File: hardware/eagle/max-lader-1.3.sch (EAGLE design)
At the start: 69 parts, among them IC1 OPA343, IC2 LM385-2.5, IC3 ICL 7667, IC4 7805, IC5 MEGA168-P, Q1 IRF4905, Q2 16MHz, Q3 IRFZ 48N, Q4 IRFZ 48N

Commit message: eagle files
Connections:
- net N$1 renamed INPUT_GATE
- net N$10 renamed BOOST_GATE
- net N$15 renamed BOOST_CTRL
- net N$3 renamed BUCK_CTRL
- net N$4 renamed BUCK_GATE
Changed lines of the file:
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@@
 <?xml version="1.0" encoding="utf-8"?>
 <!DOCTYPE eagle SYSTEM "eagle.dtd">
-<eagle version="6.5.0">
+<eagle version="7.7.0">
 <drawing>
 <settings>
@@
 </segment>
 </net>
-<net name="N$15" class="0">
+<net name="BOOST_CTRL" class="0">
 <segment>
 <wire x1="93.98" y1="17.78" x2="93.98" y2="40.64" width="0.1524" layer="91"/>
@@
 </segment>
 </net>
-<net name="N$1" class="0">
+<net name="INPUT_GATE" class="0">
 <segment>
 <wire x1="-17.78" y1="48.26" x2="-12.7" y2="48.26" width="0.1524" layer="91"/>
@@
 </segment>
 </net>
-<net name="N$10" class="0">
+<net name="BOOST_GATE" class="0">
 <segment>
 <wire x1="93.98" y1="53.34" x2="101.6" y2="53.34" width="0.1524" layer="91"/>
@@
 </segment>
 </net>
-<net name="N$4" class="0">
+<net name="BUCK_GATE" class="0">
 <segment>
 <wire x1="73.66" y1="78.74" x2="66.04" y2="78.74" width="0.1524" layer="91"/>
@@
 </segment>
 </net>
-<net name="N$3" class="0">
+<net name="BUCK_CTRL" class="0">
 <segment>
 <wire x1="66.04" y1="38.1" x2="66.04" y2="22.86" width="0.1524" layer="91"/>

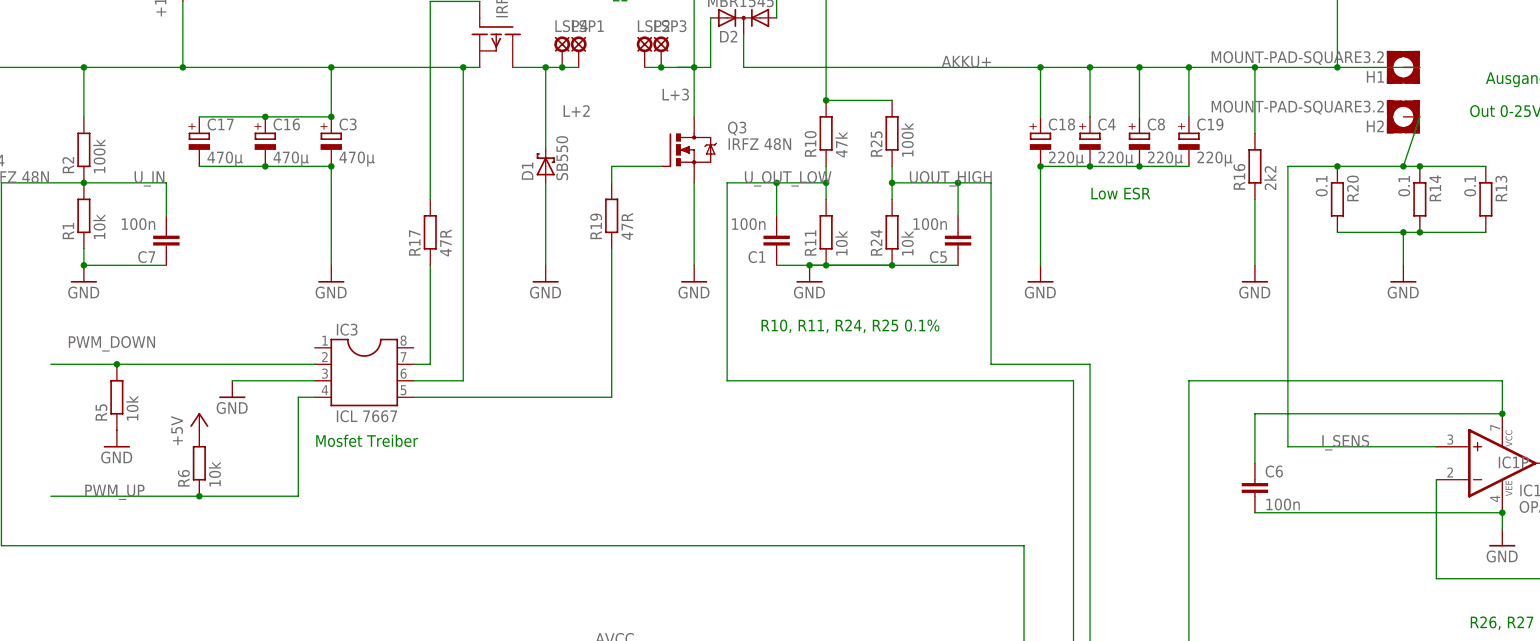
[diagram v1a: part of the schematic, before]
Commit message: layout version 1.5 with 1k protection resistors for icl7667 failure on overvoltage, it will kill the atmega168 without
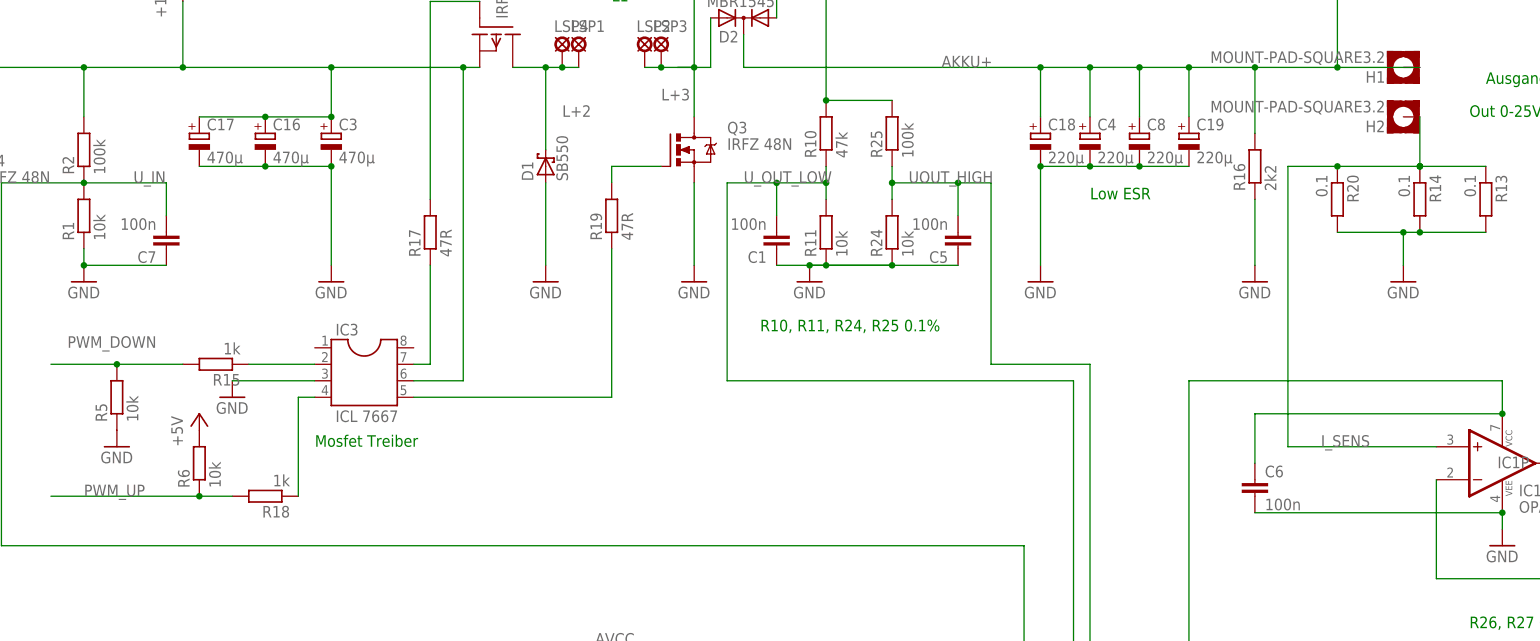
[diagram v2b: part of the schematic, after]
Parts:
- added R15, R18: 1k, rcl:R-EU_R0805
- R22, R23, R5, R6, R8: device rcl:R-EU_0207/10 -> rcl:R-EU_R0805
- R7: device rcl:R-EU_0207/15 -> rcl:R-EU_R0805
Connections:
- new net N$1: IC3.4, R18.1
- new net N$3: IC3.2, R15.1
- net PWM_DOWN: now also R15.2; no longer IC3.2
- net PWM_UP: now also R18.2; no longer IC3.4
